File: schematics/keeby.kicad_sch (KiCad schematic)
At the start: 151 parts, among them SW1 SW_Push, SW10 SW_Push, SW11 SW_Push, SW12 SW_Push, SW13 SW_Push, SW14 SW_Push, SW15 SW_Push, SW16 SW_Push, SW17 SW_Push, SW18 SW_Push, SW19 SW_Push, SW2 SW_Push, SW20 SW_Push, SW21 SW_Push, SW22 SW_Push, SW23 SW_Push, SW24 SW_Push, SW25 SW_Push, SW26 SW_Push, SW27 SW_Push, SW28 SW_Push, SW29 SW_Push, SW3 SW_Push, SW30 SW_Push, SW31 SW_Push, SW32 SW_Push, SW33 SW_Push, SW34 SW_Push, SW35 SW_Push, SW36 SW_Push, SW37 SW_Push, SW38 SW_Push, SW39 SW_Push, SW4 SW_Push, SW40 SW_Push, SW41 SW_Push, SW42 SW_Push, SW43 SW_Push, SW44 SW_Push, SW45 SW_Push, SW46 SW_Push, SW47 SW_Push, SW48 SW_Push, SW49 SW_Push, SW5 SW_Push, SW50 SW_Push, SW51 SW_Push, SW52 SW_Push, SW53 SW_Push, SW54 SW_Push, SW55 SW_Push, SW56 SW_Push, SW57 SW_Push, SW58 SW_Push, SW59 SW_Push, SW6 SW_Push, SW60 SW_Push, SW61 SW_Push, SW62 SW_Push, SW63 SW_Push, SW64 SW_Push, SW65 SW_Push, SW66 SW_Push, SW67 SW_Push, SW68 SW_Push, SW7 SW_Push, SW8 SW_Push, SW9 SW_Push, U1 SuperMini nRF52840, U2 MCP23017x-x-SP

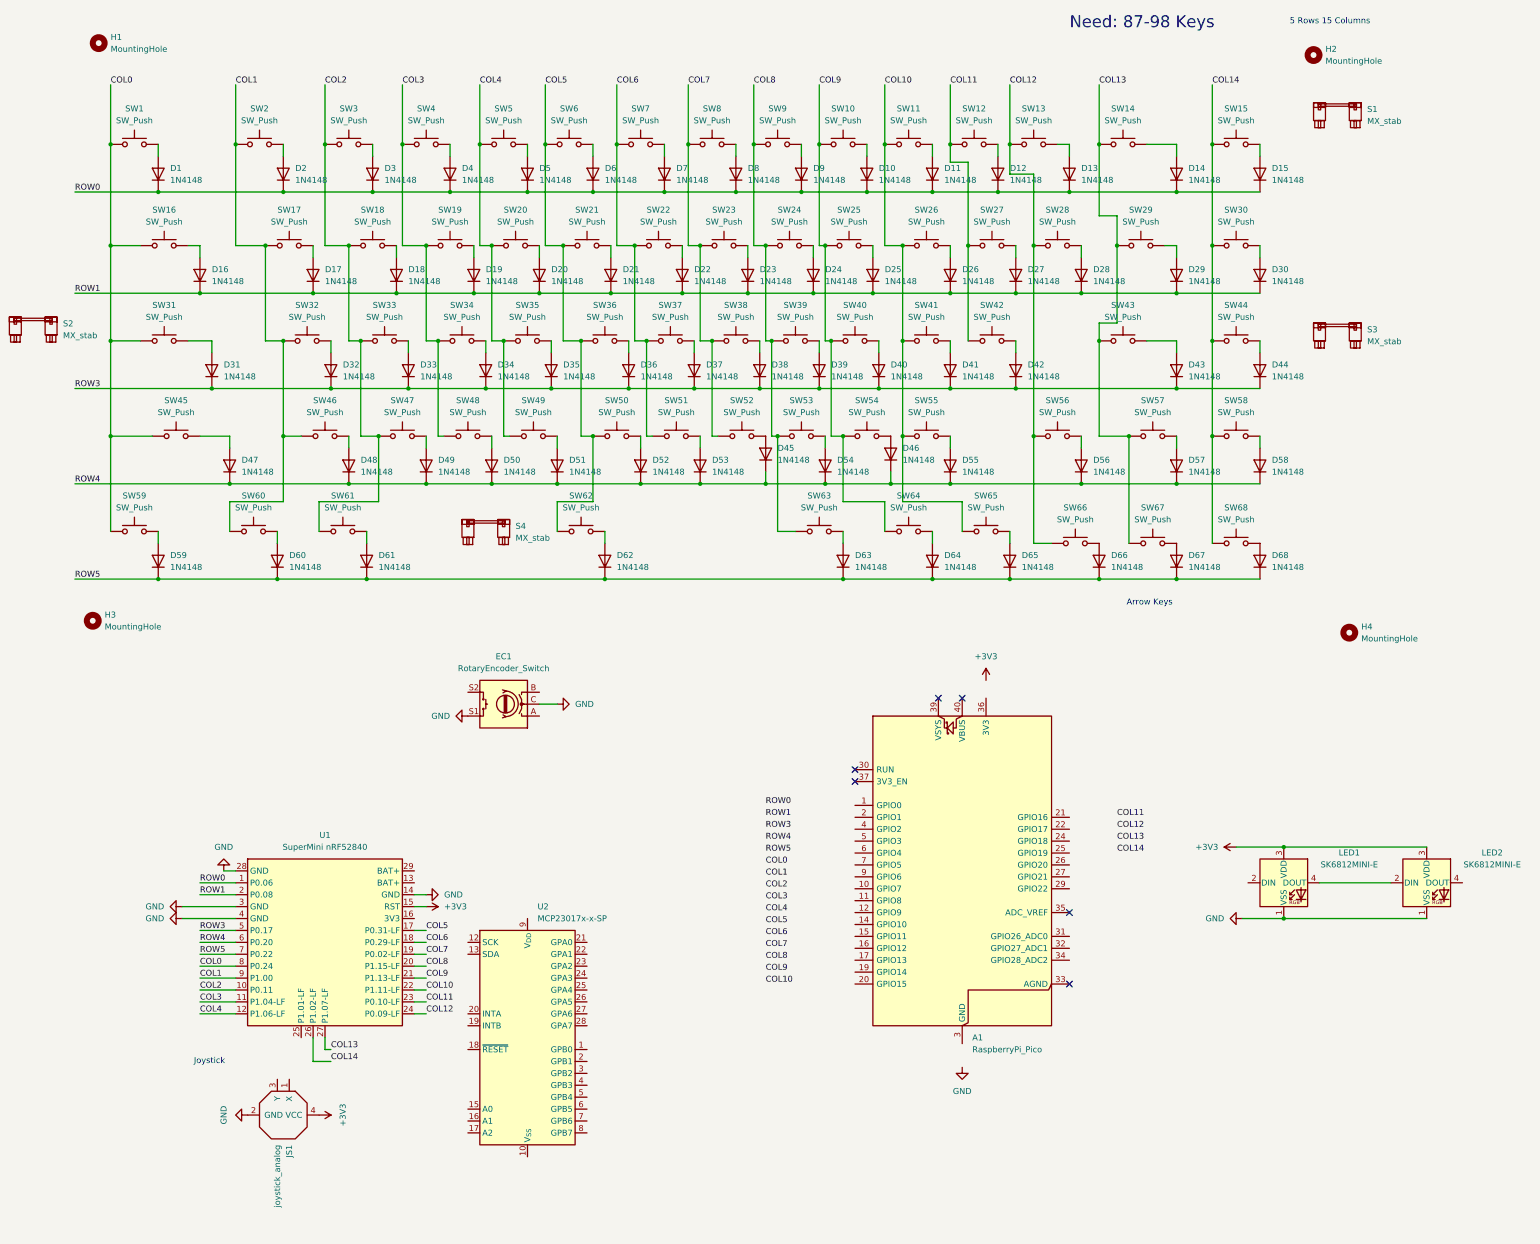
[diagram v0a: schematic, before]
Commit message: added nrf 3d models and all the other needed models
models and nrf
the commit before had a few things merged together that I actually wanted to separate into different commits
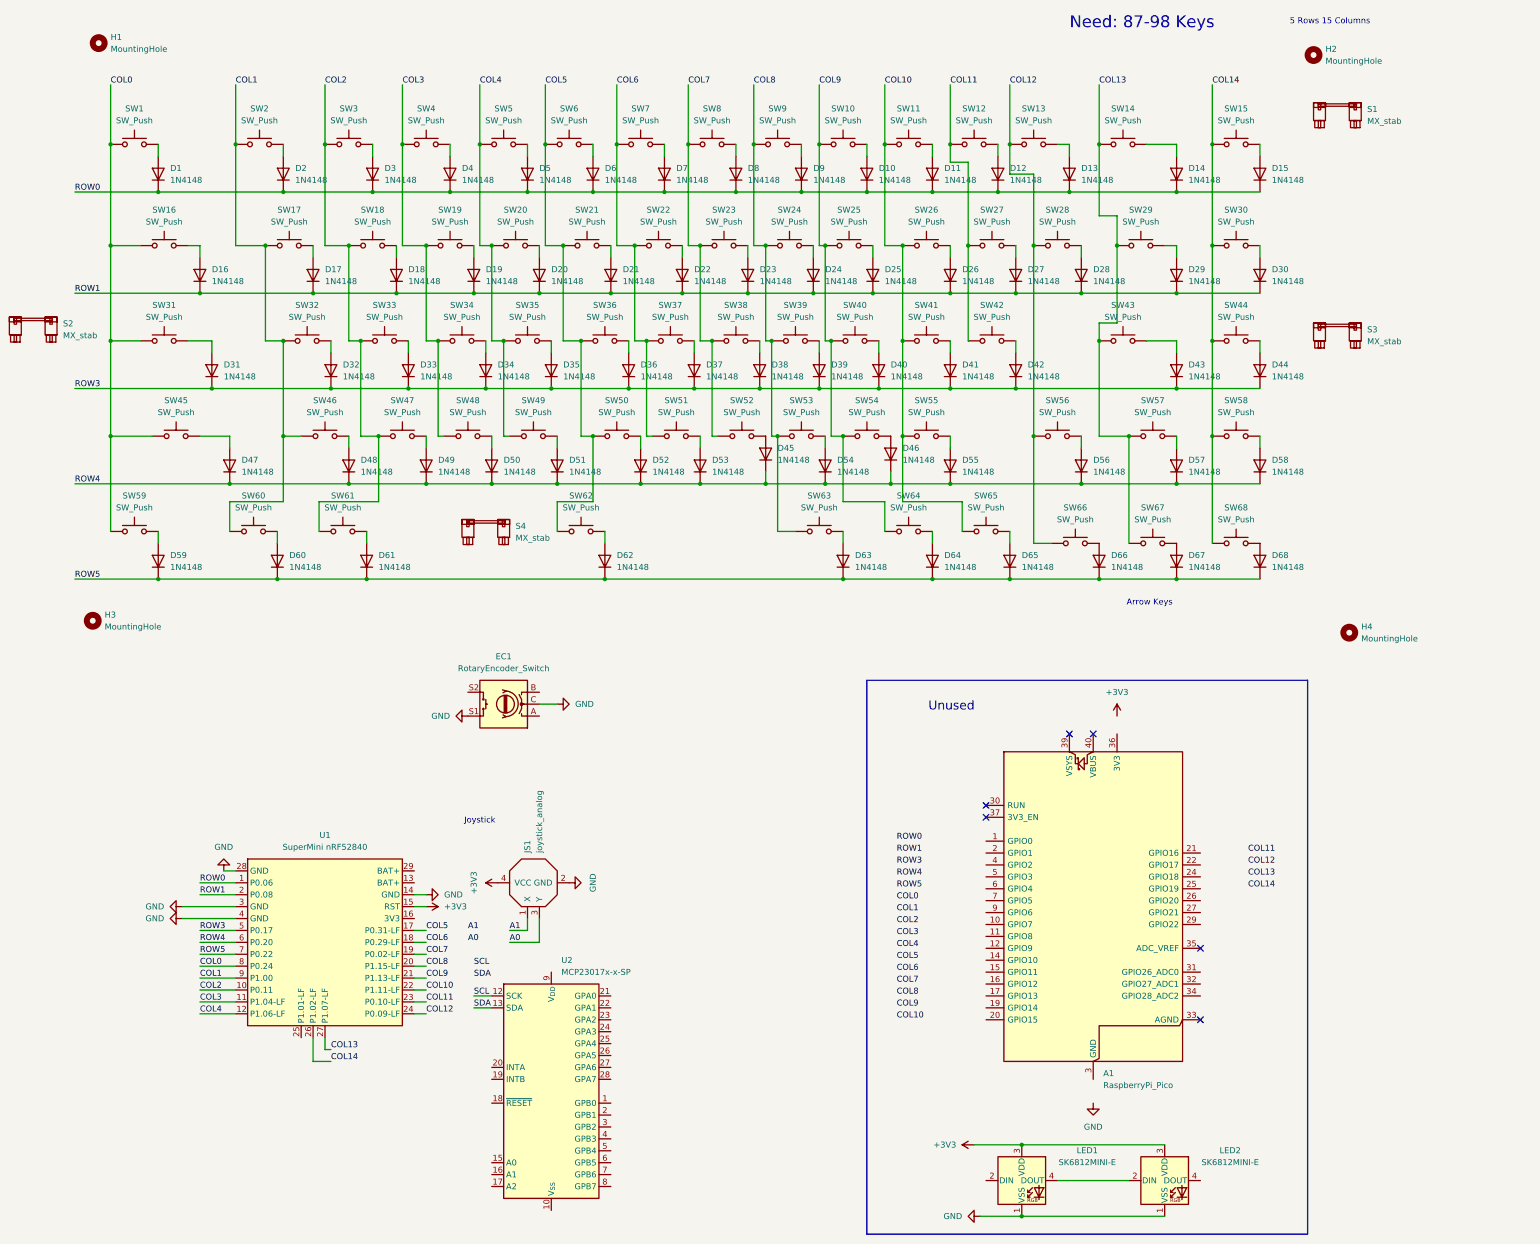
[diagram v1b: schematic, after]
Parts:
- H1, H2, H3, H4: footprint (none) -> MountingHole:MountingHole_2.1mm
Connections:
- net SCL: now reaches U2.12 (SCK)
- net SDA: now reaches U2.13 (SDA)
- net A1: now reaches JS1.1 (X)
- net A0: now reaches JS1.3 (Y)
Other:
- note added: "Unused"
- moved on the sheet: A1, JS1, LED1, LED2, U2

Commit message: help
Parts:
- added SW69: SW_Slide_DPDT, symbol Switch:SW_Slide_DPDT
- added SW70: SW_SPST, symbol Switch:SW_SPST
- H1, H2, H3, H4: footprint MountingHole:MountingHole_2.1mm -> MountingHole:MountingHole_2.2mm_M2
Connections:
- net +3V3: now also U1.16 (3V3); no longer U1.15 (RST)
- net COL0: no longer SW1.1, SW16.1, SW31.1, SW45.1, SW59.1, U1.8 (P0.24)
- net COL1: now also SW1.1, SW16.1, SW31.1, SW45.1, SW59.1, U1.1 (P0.06); no longer SW17.1, SW2.1, SW32.1, SW46.1, SW60.1, U1.9 (P1.00)
- net COL10: now also SW10.1, SW25.1, SW40.1, SW54.1, SW64.1, U1.12 (P1.06-LF); no longer SW11.1, SW26.1, SW41.1, SW55.1, SW65.1, U1.22 (P1.11-LF)
- net COL11: now also SW11.1, SW26.1, SW41.1, SW55.1, SW65.1, U1.24 (P0.09-LF); no longer SW12.1, SW27.1, SW42.1, U1.23 (P0.10-LF)
- net COL12: now also SW12.1, SW27.1, SW42.1, U1.23 (P0.10-LF); no longer SW13.1, SW28.1, SW56.1, SW66.1, U1.24 (P0.09-LF)
- net COL13: now also SW13.1, SW28.1, SW56.1, SW66.1, U1.22 (P1.11-LF); no longer SW14.1, SW29.1, SW43.1, SW57.1, SW67.1, U1.27 (P1.07-LF)
- net COL14: now also SW14.1, SW29.1, SW43.1, SW57.1, SW67.1, U1.27 (P1.07-LF); no longer SW15.1, SW30.1, SW44.1, SW58.1, SW68.1, U1.26 (P1.02-LF)
- net COL2: now also SW17.1, SW2.1, SW32.1, SW46.1, SW60.1, U1.2 (P0.08); no longer SW18.1, SW3.1, SW33.1, SW47.1, SW61.1, U1.10 (P0.11)
- net COL3: now also SW18.1, SW3.1, SW33.1, SW47.1, SW61.1, U1.5 (P0.17); no longer SW19.1, SW34.1, SW4.1, SW48.1, U1.11 (P1.04-LF)
- net COL4: now also SW19.1, SW34.1, SW4.1, SW48.1, U1.6 (P0.20); no longer SW20.1, SW35.1, SW49.1, SW5.1, U1.12 (P1.06-LF)
- net COL5: now also SW20.1, SW35.1, SW49.1, SW5.1, U1.7 (P0.22); no longer SW21.1, SW36.1, SW50.1, SW6.1, SW62.1, U1.17 (P0.31-LF)
- net COL6: now also SW21.1, SW36.1, SW50.1, SW6.1, SW62.1, U1.8 (P0.24); no longer SW22.1, SW37.1, SW51.1, SW7.1, U1.18 (P0.29-LF)
- net COL7: now also SW22.1, SW37.1, SW51.1, SW7.1, U1.9 (P1.00); no longer SW23.1, SW38.1, SW52.1, SW8.1, U1.19 (P0.02-LF)
- net COL8: now also SW23.1, SW38.1, SW52.1, SW8.1, U1.10 (P0.11); no longer SW24.1, SW39.1, SW53.1, SW63.1, SW9.1, U1.20 (P1.15-LF)
- net COL9: now also SW24.1, SW39.1, SW53.1, SW63.1, SW9.1, U1.11 (P1.04-LF); no longer SW10.1, SW25.1, SW40.1, SW54.1, SW64.1, U1.21 (P1.13-LF)
- net ROW0: no longer D1.1 (K), D10.1 (K), D11.1 (K), D12.1 (K), D13.1 (K), D14.1 (K), D15.1 (K), D2.1 (K), D3.1 (K), D4.1 (K), D5.1 (K), D6.1 (K), D7.1 (K), D8.1 (K), D9.1 (K), U1.1 (P0.06)
- net ROW1: now also D1.1 (K), D10.1 (K), D11.1 (K), D12.1 (K), D13.1 (K), D14.1 (K), D15.1 (K), D2.1 (K), D3.1 (K), D4.1 (K), D5.1 (K), D6.1 (K), D7.1 (K), D8.1 (K), D9.1 (K), U1.21 (P1.13-LF); no longer D16.1 (K), D17.1 (K), D18.1 (K), D19.1 (K), D20.1 (K), D21.1 (K), D22.1 (K), D23.1 (K), D24.1 (K), D25.1 (K), D26.1 (K), D27.1 (K), D28.1 (K), D29.1 (K), D30.1 (K), U1.2 (P0.08)
- net ROW3: now also U1.19 (P0.02-LF); no longer U1.5 (P0.17)
- net ROW4: now also U1.18 (P0.29-LF); no longer U1.6 (P0.20)
- net ROW5: now also U1.17 (P0.31-LF); no longer U1.7 (P0.22)
- new net COL15: SW15.1, SW30.1, SW44.1, SW58.1, SW68.1, U1.26 (P1.02-LF)
- new net ROW2: D16.1 (K), D17.1 (K), D18.1 (K), D19.1 (K), D20.1 (K), D21.1 (K), D22.1 (K), D23.1 (K), D24.1 (K), D25.1 (K), D26.1 (K), D27.1 (K), D28.1 (K), D29.1 (K), D30.1 (K), U1.20 (P1.15-LF)
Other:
- note added: "Ordered specifically to simplify routing"
- moved on the sheet: EC1, JS1, U1, U2

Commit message: a bunch of messy routing and wiring
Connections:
- net +3V3: now also U2.18 (~{RESET}), U2.9 (V_{DD})
- net A0: now also U2.15 (A0)
- net A1: now also U2.16 (A1)
- net GND: now also U2.10 (V_{SS})
- net at EC1.A: now also U2.2 (GPB1)
- net at EC1.B: now also U2.3 (GPB2)
- net at EC1.S2: now also U2.1 (GPB0)
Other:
- moved on the sheet: EC1

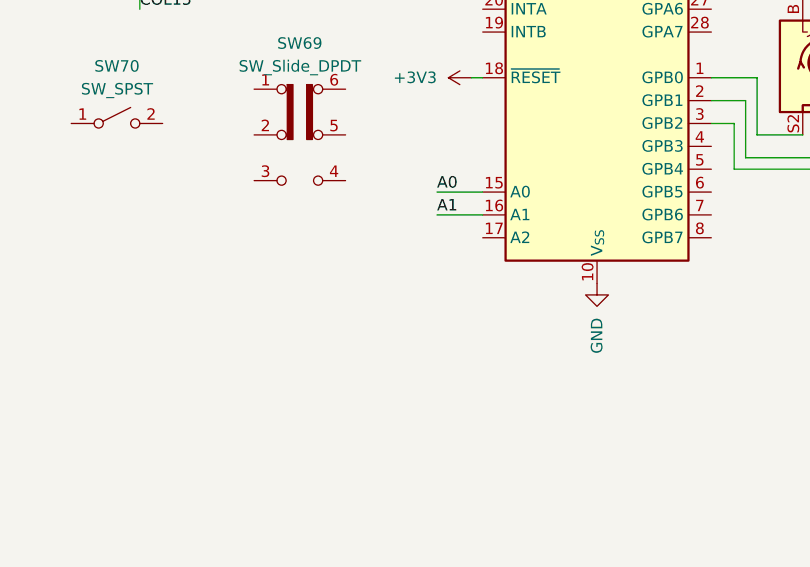
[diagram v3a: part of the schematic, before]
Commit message: pcb export 1 but im gonna change it anyway
help im going to shift the microcontroller up a bit
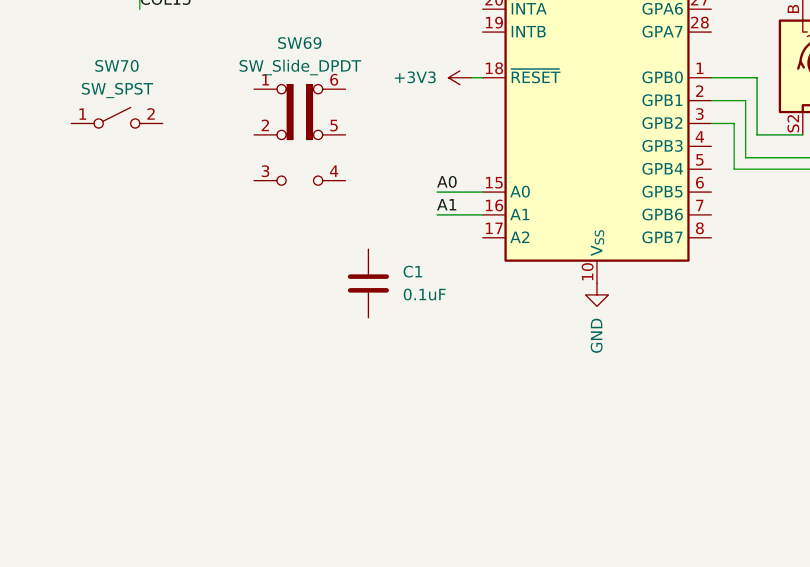
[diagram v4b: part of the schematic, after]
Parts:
- added C1: 0.1uF, symbol Device:C
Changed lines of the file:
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@@
+	)
+	(symbol
+		(lib_id "Device:C")
+		(at 121.92 241.3 0)
+		(unit 1)
+		(body_style 1)
+		(exclude_from_sim no)
+		(in_bom yes)
+		(on_board yes)
+		(in_pos_files yes)
+		(dnp no)
+		(fields_autoplaced yes)
+		(property "Reference" "C1"
+			(at 125.73 240.0299 0)
+			(show_name no)
+			(do_not_autoplace no)
+			(effects
+				(font
+					(size 1.27 1.27)
+				)
+				(justify left)
+			)
+		)
+		(property "Value" "0.1uF"
+			(at 125.73 242.5699 0)
+			(show_name no)
+			(do_not_autoplace no)
+			(effects
+				(font
+					(size 1.27 1.27)
+				)
+				(justify left)
+			)
+		)
+		(property "Footprint" ""
+			(at 122.8852 245.11 0)
+			(hide yes)
+			(show_name no)
+			(do_not_autoplace no)
+			(effects
+				(font
+					(size 1.27 1.27)
+				)
+			)
+		)
+		(property "Datasheet" ""
+			(at 121.92 241.3 0)
+			(hide yes)
+			(show_name no)
+			(do_not_autoplace no)
+			(effects
+				(font
+					(size 1.27 1.27)
+				)
+			)
+		)
+		(property "Description" "Unpolarized capacitor"
+			(at 121.92 241.3 0)
+			(hide yes)
+			(show_name no)
+			(do_not_autoplace no)
+			(effects
+				(font
+					(size 1.27 1.27)
+				)
+			)
+		)
+		(pin "1"
+		)
+		(pin "2"
+		)
+		(instances
+			(project "keeby"
+				(path "/cc31f2e4-f6f2-47ce-9230-2538505f0030"
+					(reference "C1")
+					(unit 1)
+				)
+			)
+		)
 	)
 	(symbol
